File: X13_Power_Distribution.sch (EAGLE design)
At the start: 38 parts, among them Y1 ECS-80-S-4X

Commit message: Made some slight changes
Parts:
- removed U$4: IRF1018EPBF, IRF1018EPBF_PowerDistribution_NMOS:IRF1018EPBF
- added D5: (no value), SparkFun-LED:LED0603
- added R4: 470, SparkFun-Resistors:RESISTOR0603
- added U$6: IRF1018EPBF, Reverse_Voltage_NMOS:IRF1018EPBF
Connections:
- new net N$8: D5.A, R4.1
- net +12V: now also R4.2
- net GND: now also D5.C, U$6.S; no longer U$4.S
- net N$3: now also U$6.G; no longer U$4.G
- net N$4: now also U$6.D; no longer U$4.D
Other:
- note added: "REVERSE VOLTAGE PROTECTION"
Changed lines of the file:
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@@
 <attribute name="SPICEPREFIX" value="R"/>
 </part>
-<part name="U$4" library="IRF1018EPBF_PowerDistribution_NMOS" deviceset="IRF1018EPBF" device=""/>
 <part name="R3" library="SparkFun-Resistors" library_urn="urn:adsk.eagle:library:532" deviceset="RESISTOR" device="0603" package3d_urn="urn:adsk.eagle:package:39650@1/1" value=" "/>
 <part name="D4" library="diode" library_urn="urn:adsk.eagle:library:210" deviceset="DIODE-" device="SOD123" package3d_urn="urn:adsk.eagle:package:43420/1"/>
@@
 <part name="H3" library="SparkFun-Hardware" library_urn="urn:adsk.eagle:library:519" deviceset="STAND-OFF" device="" package3d_urn="urn:adsk.eagle:package:38630/1"/>
 <part name="H4" library="SparkFun-Hardware" library_urn="urn:adsk.eagle:library:519" deviceset="STAND-OFF" device="" package3d_urn="urn:adsk.eagle:package:38630/1"/>
+<part name="D5" library="SparkFun-LED" library_urn="urn:adsk.eagle:library:529" deviceset="LED" device="0603" package3d_urn="urn:adsk.eagle:package:39354/1"/>
+<part name="R4" library="SparkFun-Resistors" library_urn="urn:adsk.eagle:library:532" deviceset="RESISTOR" device="0603" package3d_urn="urn:adsk.eagle:package:39650@1/1" value="470"/>
+<part name="U$6" library="Reverse_Voltage_NMOS" deviceset="IRF1018EPBF" device=""/>
 </parts>
 <sheets>
@@
 <text x="74.93" y="232.41" size="2.54" layer="91">TURN OFF/ON CIRCUIT</text>
 <text x="29.21" y="232.41" size="2.54" layer="91">OR-ING DIODES</text>
-<text x="142.24" y="232.41" size="2.54" layer="91">TURN OFF/ON CIRCUIT</text>
+<text x="142.24" y="232.41" size="2.54" layer="91">REVERSE VOLTAGE PROTECTION</text>
 </plain>
 <instances>
@@
 <attribute name="VALUE" x="106.934" y="212.09" size="1.778" layer="96" font="vector" rot="R90" align="top-center"/>
 </instance>
-<instance part="U$4" gate="G$1" x="173.99" y="198.12" smashed="yes" rot="R270">
-<attribute name="NAME" x="173.99" y="193.04" size="1.778" layer="95" font="vector" rot="R270"/>
-<attribute name="VALUE" x="171.45" y="193.04" size="1.778" layer="96" font="vector" rot="R270"/>
-</instance>
 <instance part="R3" gate="G$1" x="160.02" y="200.66" smashed="yes" rot="R90">
 <attribute name="NAME" x="158.496" y="200.66" size="1.778" layer="95" font="vector" rot="R90" align="bottom-center"/>
@@
 <attribute name="NAME" x="165.8874" y="212.09" size="1.778" layer="95" rot="R90"/>
 <attribute name="VALUE" x="168.6814" y="212.09" size="1.778" layer="96" rot="R90"/>
+</instance>
+<instance part="D5" gate="G$1" x="274.32" y="144.78" smashed="yes">
+<attribute name="NAME" x="270.891" y="140.208" size="1.778" layer="95" font="vector" rot="R90"/>
+<attribute name="VALUE" x="276.225" y="140.208" size="1.778" layer="96" font="vector" rot="R90" align="top-left"/>
+</instance>
+<instance part="R4" gate="G$1" x="274.32" y="160.02" smashed="yes" rot="R90">
+<attribute name="NAME" x="272.796" y="160.02" size="1.778" layer="95" font="vector" rot="R90" align="bottom-center"/>
+<attribute name="VALUE" x="275.844" y="160.02" size="1.778" layer="96" font="vector" rot="R90" align="top-center"/>
+</instance>
+<instance part="U$6" gate="G$1" x="172.72" y="198.12" smashed="yes" rot="R270">
+<attribute name="NAME" x="172.72" y="193.04" size="1.778" layer="95" font="vector" rot="R270"/>
+<attribute name="VALUE" x="170.18" y="193.04" size="1.778" layer="96" font="vector" rot="R270"/>
 </instance>
 </instances>
@@
 <wire x1="54.61" y1="209.55" x2="54.61" y2="217.17" width="0.1524" layer="91"/>
 <label x="54.61" y="217.17" size="1.778" layer="95" rot="R90" xref="yes"/>
+</segment>
+<segment>
+<pinref part="R4" gate="G$1" pin="2"/>
+<wire x1="274.32" y1="165.1" x2="274.32" y2="170.18" width="0.1524" layer="91"/>
+<label x="274.32" y="170.18" size="1.778" layer="95" rot="R180" xref="yes"/>
 </segment>
 </net>
@@
 <wire x1="160.02" y1="205.74" x2="166.37" y2="205.74" width="0.1524" layer="91"/>
 <wire x1="166.37" y1="205.74" x2="166.37" y2="207.01" width="0.1524" layer="91"/>
-<pinref part="U$4" gate="G$1" pin="G"/>
-<wire x1="171.45" y1="203.2" x2="171.45" y2="205.74" width="0.1524" layer="91"/>
-<wire x1="171.45" y1="205.74" x2="166.37" y2="205.74" width="0.1524" layer="91"/>
-<junction x="166.37" y="205.74"/>
+<wire x1="166.37" y1="205.74" x2="170.18" y2="205.74" width="0.1524" layer="91"/>
+<pinref part="U$6" gate="G$1" pin="G"/>
+<wire x1="170.18" y1="205.74" x2="170.18" y2="203.2" width="0.1524" layer="91"/>
 </segment>
 </net>
@@
 <segment>
 <pinref part="R3" gate="G$1" pin="1"/>
-<pinref part="U$4" gate="G$1" pin="S"/>
-<wire x1="160.02" y1="195.58" x2="168.91" y2="195.58" width="0.1524" layer="91"/>
+<wire x1="160.02" y1="195.58" x2="167.64" y2="195.58" width="0.1524" layer="91"/>
+<wire x1="167.64" y1="195.58" x2="168.91" y2="195.58" width="0.1524" layer="91"/>
 <wire x1="160.02" y1="195.58" x2="153.67" y2="195.58" width="0.1524" layer="91"/>
 <junction x="160.02" y="195.58"/>
 <label x="153.67" y="195.58" size="1.778" layer="95" rot="R180" xref="yes"/>
+<pinref part="U$6" gate="G$1" pin="S"/>
+<junction x="167.64" y="195.58"/>
+</segment>
+<segment>
+<pinref part="D5" gate="G$1" pin="C"/>
+<wire x1="274.32" y1="127" x2="274.32" y2="139.7" width="0.1524" layer="91"/>
+<label x="274.32" y="127" size="1.778" layer="95" rot="R180" xref="yes"/>
 </segment>
 </net>
@@
 </segment>
 </net>
+<net name="N$8" class="0">
+<segment>
+<pinref part="D5" gate="G$1" pin="A"/>
+<pinref part="R4" gate="G$1" pin="1"/>
+<wire x1="274.32" y1="147.32" x2="274.32" y2="154.94" width="0.1524" layer="91"/>
+</segment>
+</net>
 <net name="N$4" class="0">
 <segment>
-<pinref part="U$4" gate="G$1" pin="D"/>
-<wire x1="179.07" y1="195.58" x2="182.88" y2="195.58" width="0.1524" layer="91"/>
-</segment>
-</net>
+<pinref part="U$6" gate="G$1" pin="D"/>
+<wire x1="177.8" y1="195.58" x2="182.88" y2="195.58" width="0.1524" layer="91"/>
+</segment>
+</net>

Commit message: goodbye microcontroller
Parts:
- removed C1, C10, C2, C3, C4, C5, C6, C7, C8, C9: 4.7uF, SparkFun-Capacitors:4.7UF0603
- removed C11: 0.1uF, SparkFun-Capacitors:0.1UF-0603-25V-(+80/-20%)
- removed D6: (no value), SparkFun-LED:LED0603
- removed H1, H2, H3, H4: STAND-OFF, SparkFun-Hardware:STAND-OFF
- removed R10, R11: 60, SparkFun-Resistors:1KOHM-0603-1/10W-1%
- removed R5, R6, R7: 1k, SparkFun-Resistors:1KOHM-0603-1/10W-1%
- removed R8: 470, SparkFun-Resistors:RESISTOR0603
- removed RESET: SWITCH, DiscreteComponents:SWITCH
- removed SV1: (no value), con-lsta:FE05-1
- removed U$5: STM32F042K6T6, PI_Shield_Library:STM32F042K6T6
- removed U$8: TCAN337D, PI_Shield_Library:TCAN337D
- removed Y1: ECS-80-S-4X, ECS-80-S-4X:ECS-80-S-4X
- added J1, J2, J3, J4: (no value), SparkFun-Connectors:BANANA_CONN
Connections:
- removed net +3V3: C1.1, C10.1, C2.1, C3.1, C4.1, C5.1, C6.1, R6.2, SV1.5, U$5.VDD, U$5.VDDA, U$5.VDDIO2, U$8.VCC
- removed net 3V3GND: C1.2, C10.2, C11.1, C2.2, C3.2, C4.2, C5.2, C6.2, C7.2, C8.2, C9.2, D6.C, RESET.P$1, SV1.3, U$5.PB8-BOOT0, U$5.VSS, U$5.VSS1, U$8.GND
- removed net ALERT: U$5.PB7
- removed net CAN_H: R10.2, U$8.CANH
- removed net CAN_L: R11.1, U$8.CANL
- removed net CAN_RX: U$5.PA11, U$8.RXD
- removed net CAN_TX: U$5.PA12, U$8.TXD
- removed net CLK: U$5.PA9
- removed net DATA: U$5.PA10
- removed net LED: R8.2, U$5.PA15
- removed net N$24: D6.A, R8.1
- removed net N$5: C11.2, R10.1, R11.2
- removed net N$6: C9.1, R5.1, Y1.2
- removed net N$7: C8.1, R7.1, Y1.1
- removed net NRST: C7.1, R6.1, RESET.P$2, SV1.1, U$5.NRST
- removed net OSC_IN: R7.2, U$5.PF0-OSC_IN
- removed net OSC_OUT: R5.2, U$5.PF1-OSC_OUT
- removed net SWCLK: SV1.4, U$5.PA14
- removed net SWDIO: SV1.2, U$5.PA13
- new net +48V_RAW: J1.1
- net +48V: now also J3.1
- net 48V_GND: now also J2.1, J4.1
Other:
- note added: "48 VOLT CONNECTOR"
- note added: "48 VOLT POE"
- note removed: "CAN TERMINATION"
- note removed: "CAN TRANSCEIVER"
- note removed: "Pin 1 (VDD)"
- note removed: "Pin 17 (VDDIO2)"
- note removed: "Pin 5 (VDDA)"

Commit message: Added the diodes :))
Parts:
- added D6: 30V, SparkFun-DiscreteSemi:DIODE-ZENER-BZT52C3V6S
- D1, D3: device diode:ZENER-DIODESOT23 -> SparkFun-DiscreteSemi:DIODE-ZENER-BZT52C3V6S
- D4: value (none) -> 30V; device diode:DIODE-SOD123 -> SparkFun-DiscreteSemi:DIODE-ZENER-BZT52C3V6S
- R1, R3: value (none) -> 1M
- R2: value (none) -> 10k
- renumbered R4 to R5
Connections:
- new net N$5: D4.C, D6.A
- net +48V: now also D1.C; no longer D3.C
- net 48_RAW: now also D6.C; no longer D4.C
- net N$1: now also D1.A, D3.C; no longer D1.C, D3.A
- net N$2: now also D3.A; no longer D1.A
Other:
- moved on the sheet: R3, U$6

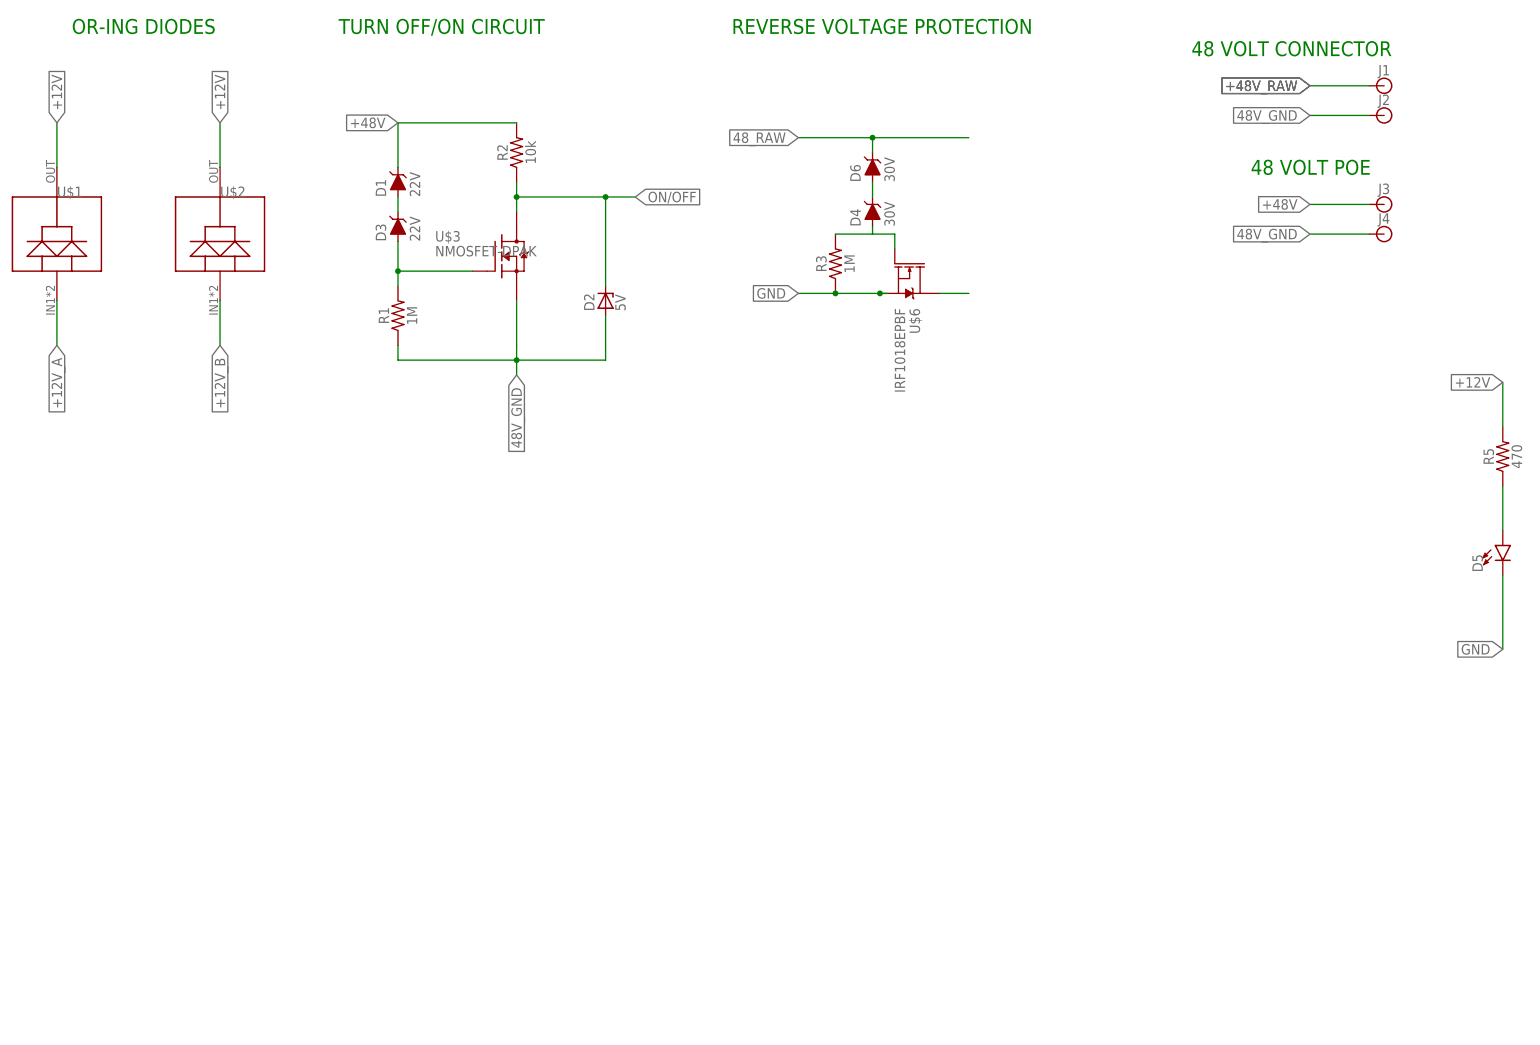
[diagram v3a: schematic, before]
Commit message: Starting on connectors
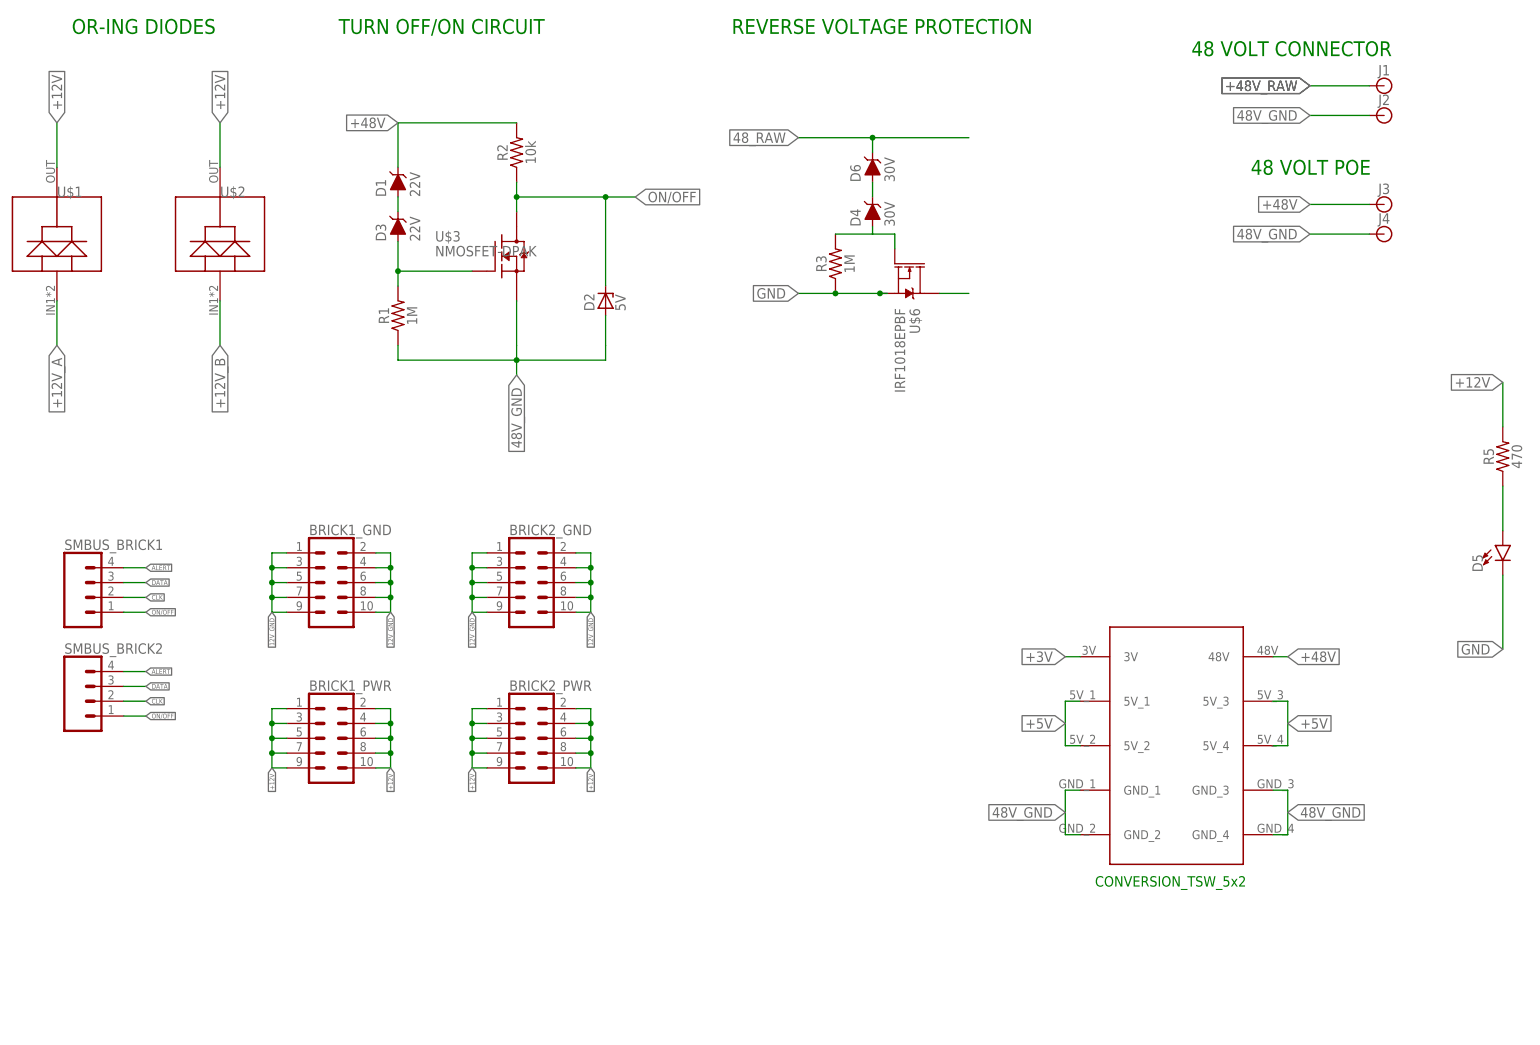
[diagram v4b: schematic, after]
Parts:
- added BRICK1_GND, BRICK1_PWR, BRICK2_GND, BRICK2_PWR: (no value), SparkFun-Connectors:CONN_05X2PTH
- added SMBUS_BRICK1, SMBUS_BRICK2: (no value), SparkFun-Connectors:CONN_04
- added U$4: DIST_TO_CONV, Dist_To_Conv_Connector:DIST_TO_CONV
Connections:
- new net +3V: U$4.3V
- new net +5V: U$4.5V_1, U$4.5V_2, U$4.5V_3, U$4.5V_4
- new net 12V_GND: BRICK1_GND.1, BRICK1_GND.10, BRICK1_GND.2, BRICK1_GND.3, BRICK1_GND.4, BRICK1_GND.5, BRICK1_GND.6, BRICK1_GND.7, BRICK1_GND.8, BRICK1_GND.9, BRICK2_GND.1, BRICK2_GND.10, BRICK2_GND.2, BRICK2_GND.3, BRICK2_GND.4, BRICK2_GND.5, BRICK2_GND.6, BRICK2_GND.7, BRICK2_GND.8, BRICK2_GND.9
- new net ALERT: SMBUS_BRICK1.4, SMBUS_BRICK2.4
- new net CLK: SMBUS_BRICK1.2, SMBUS_BRICK2.2
- new net DATA: SMBUS_BRICK1.3, SMBUS_BRICK2.3
- net +12V: now also BRICK1_PWR.1, BRICK1_PWR.10, BRICK1_PWR.2, BRICK1_PWR.3, BRICK1_PWR.4, BRICK1_PWR.5, BRICK1_PWR.6, BRICK1_PWR.7, BRICK1_PWR.8, BRICK1_PWR.9, BRICK2_PWR.1, BRICK2_PWR.10, BRICK2_PWR.2, BRICK2_PWR.3, BRICK2_PWR.4, BRICK2_PWR.5, BRICK2_PWR.6, BRICK2_PWR.7, BRICK2_PWR.8, BRICK2_PWR.9
- net +48V: now also U$4.48V
- net 48V_GND: now also U$4.GND_1, U$4.GND_2, U$4.GND_3, U$4.GND_4
- net ON/OFF: now also SMBUS_BRICK1.1, SMBUS_BRICK2.1
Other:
- note added: "CONVERSION_TSW_5x2"

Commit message: Added placeholders
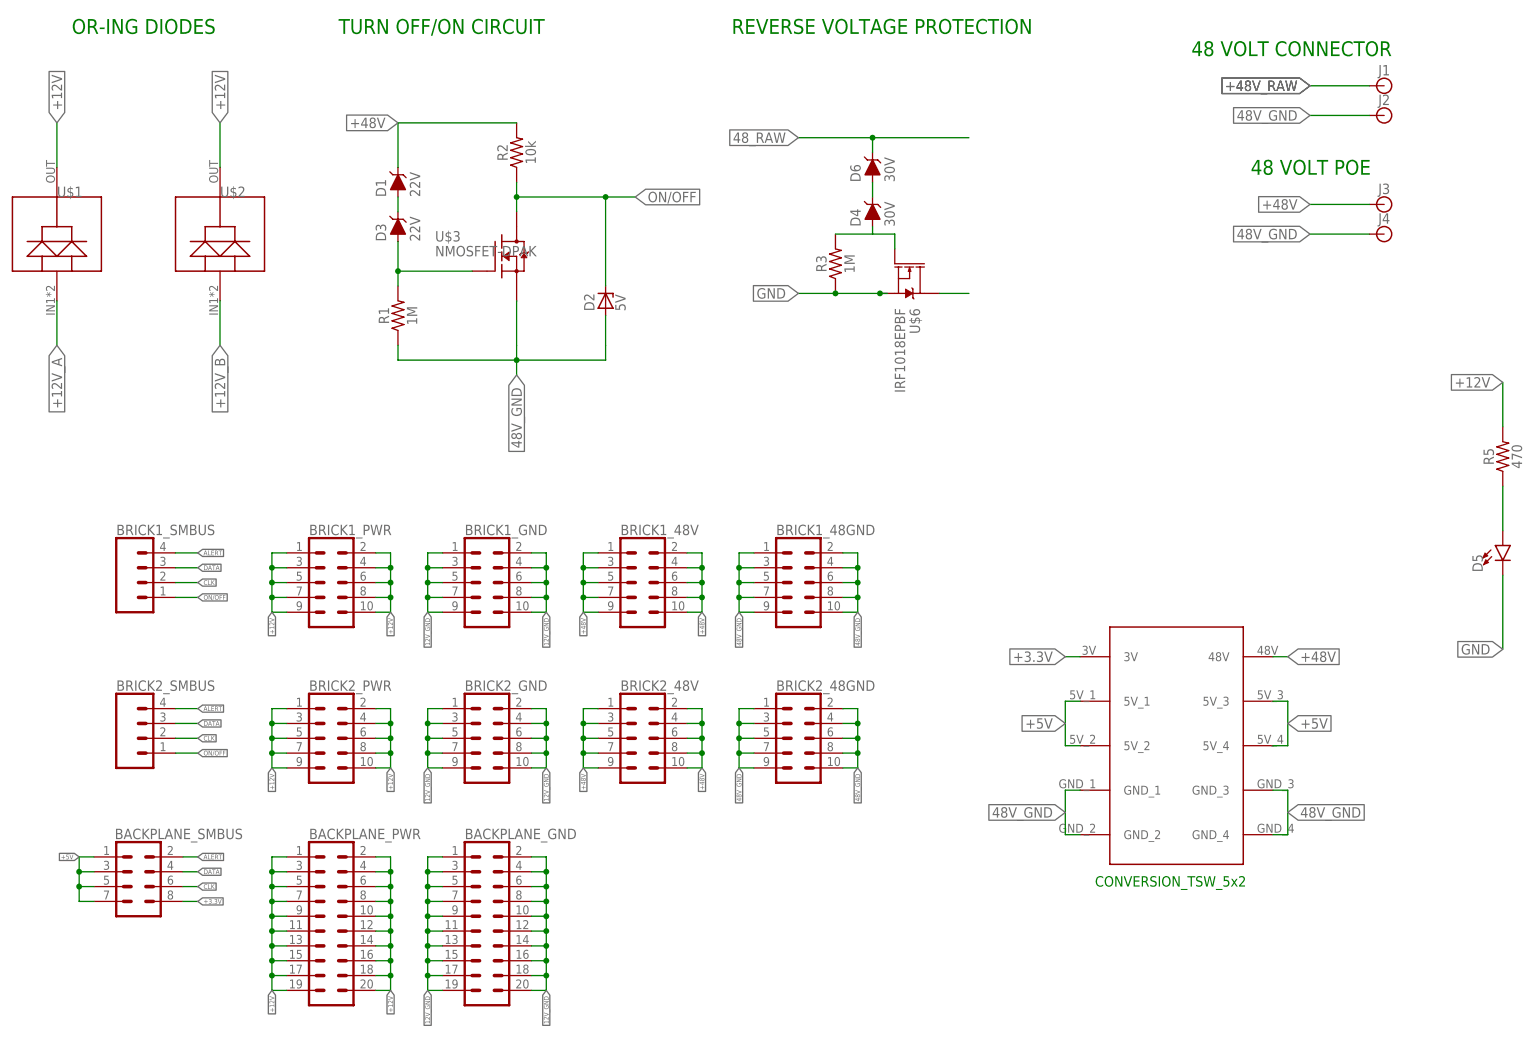
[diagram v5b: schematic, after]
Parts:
- removed SMBUS_BRICK1, SMBUS_BRICK2: (no value), SparkFun-Connectors:CONN_04
- added BACKPLANE_GND, BACKPLANE_PWR: (no value), SparkFun-Connectors:CONN_10X2
- added BACKPLANE_SMBUS: (no value), SparkFun-Connectors:CONN_04X2
- added BRICK1_48GND, BRICK1_48V, BRICK2_48GND, BRICK2_48V: (no value), SparkFun-Connectors:CONN_05X2PTH
- added BRICK1_SMBUS, BRICK2_SMBUS: (no value), SparkFun-Connectors:CONN_04
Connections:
- removed net +3V: U$4.3V
- new net +3.3V: BACKPLANE_SMBUS.8, U$4.3V
- net +12V: now also BACKPLANE_PWR.1, BACKPLANE_PWR.10, BACKPLANE_PWR.11, BACKPLANE_PWR.12, BACKPLANE_PWR.13, BACKPLANE_PWR.14, BACKPLANE_PWR.15, BACKPLANE_PWR.16, BACKPLANE_PWR.17, BACKPLANE_PWR.18, BACKPLANE_PWR.19, BACKPLANE_PWR.2, BACKPLANE_PWR.20, BACKPLANE_PWR.3, BACKPLANE_PWR.4, BACKPLANE_PWR.5, BACKPLANE_PWR.6, BACKPLANE_PWR.7, BACKPLANE_PWR.8, BACKPLANE_PWR.9
- net +48V: now also BRICK1_48V.1, BRICK1_48V.10, BRICK1_48V.2, BRICK1_48V.3, BRICK1_48V.4, BRICK1_48V.5, BRICK1_48V.6, BRICK1_48V.7, BRICK1_48V.8, BRICK1_48V.9, BRICK2_48V.1, BRICK2_48V.10, BRICK2_48V.2, BRICK2_48V.3, BRICK2_48V.4, BRICK2_48V.5, BRICK2_48V.6, BRICK2_48V.7, BRICK2_48V.8, BRICK2_48V.9
- net +5V: now also BACKPLANE_SMBUS.1, BACKPLANE_SMBUS.3, BACKPLANE_SMBUS.5, BACKPLANE_SMBUS.7
- net 12V_GND: now also BACKPLANE_GND.1, BACKPLANE_GND.10, BACKPLANE_GND.11, BACKPLANE_GND.12, BACKPLANE_GND.13, BACKPLANE_GND.14, BACKPLANE_GND.15, BACKPLANE_GND.16, BACKPLANE_GND.17, BACKPLANE_GND.18, BACKPLANE_GND.19, BACKPLANE_GND.2, BACKPLANE_GND.20, BACKPLANE_GND.3, BACKPLANE_GND.4, BACKPLANE_GND.5, BACKPLANE_GND.6, BACKPLANE_GND.7, BACKPLANE_GND.8, BACKPLANE_GND.9
- net 48V_GND: now also BRICK1_48GND.1, BRICK1_48GND.10, BRICK1_48GND.2, BRICK1_48GND.3, BRICK1_48GND.4, BRICK1_48GND.5, BRICK1_48GND.6, BRICK1_48GND.7, BRICK1_48GND.8, BRICK1_48GND.9, BRICK2_48GND.1, BRICK2_48GND.10, BRICK2_48GND.2, BRICK2_48GND.3, BRICK2_48GND.4, BRICK2_48GND.5, BRICK2_48GND.6, BRICK2_48GND.7, BRICK2_48GND.8, BRICK2_48GND.9
- net ALERT: now also BACKPLANE_SMBUS.2, BRICK1_SMBUS.4, BRICK2_SMBUS.4; no longer SMBUS_BRICK1.4, SMBUS_BRICK2.4
- net CLK: now also BACKPLANE_SMBUS.6, BRICK1_SMBUS.2, BRICK2_SMBUS.2; no longer SMBUS_BRICK1.2, SMBUS_BRICK2.2
- net DATA: now also BACKPLANE_SMBUS.4, BRICK1_SMBUS.3, BRICK2_SMBUS.3; no longer SMBUS_BRICK1.3, SMBUS_BRICK2.3
- net ON/OFF: now also BRICK1_SMBUS.1, BRICK2_SMBUS.1; no longer SMBUS_BRICK1.1, SMBUS_BRICK2.1
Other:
- moved on the sheet: BRICK1_GND, BRICK1_PWR, BRICK2_GND, BRICK2_PWR
